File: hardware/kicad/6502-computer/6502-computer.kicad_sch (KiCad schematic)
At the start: 1 part, among them U1 W65C02

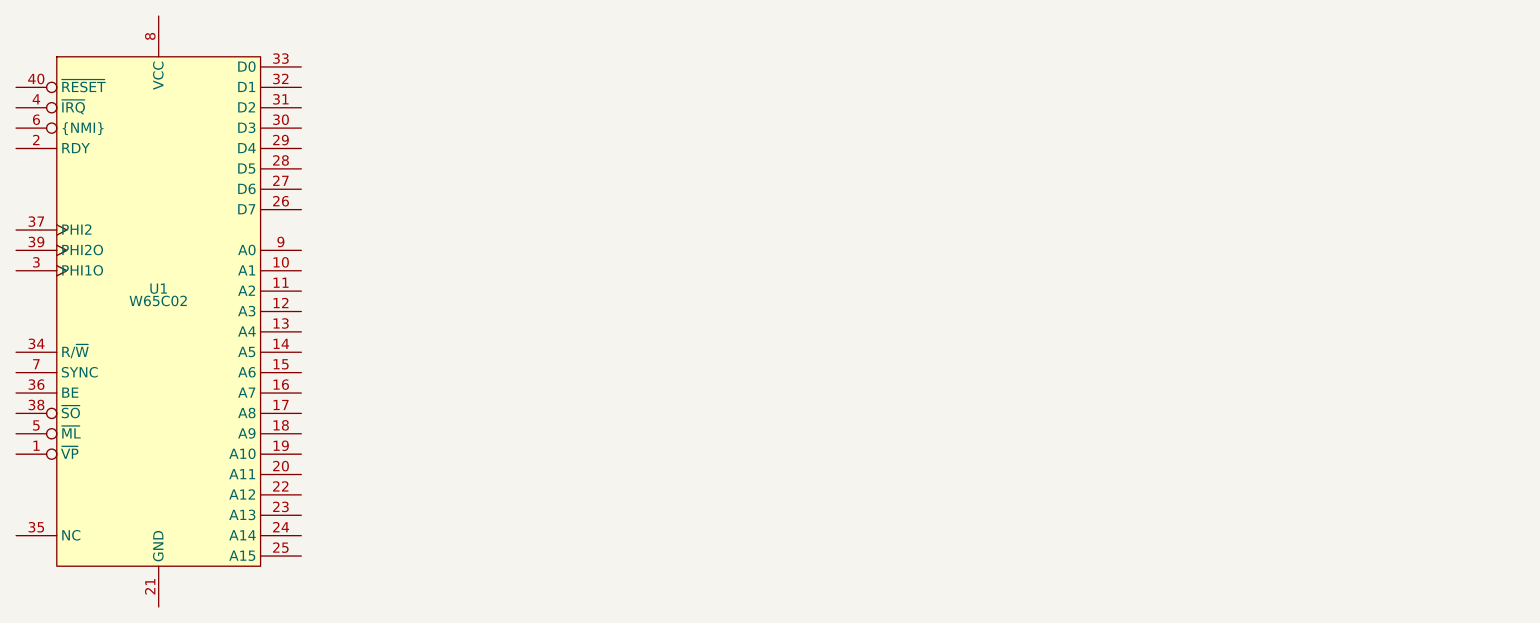
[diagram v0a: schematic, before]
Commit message: added 65c22 symbol and added it to schematics
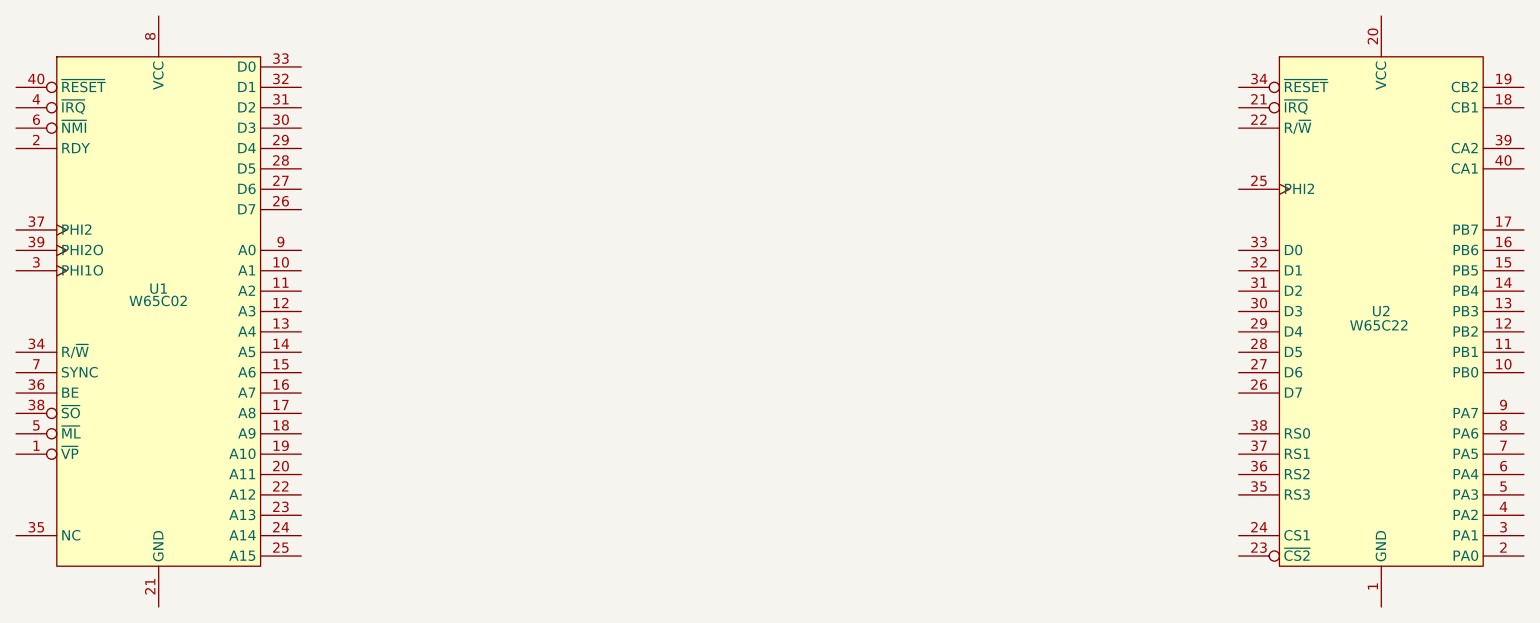
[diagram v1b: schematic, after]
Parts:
- added U2: W65C22, Package_DIP:DIP-40_W15.24mm, symbol 6502-computer:W65C22
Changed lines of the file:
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@@
 			)
+		)
+		(pin "26"
+		)
+		(pin "10"
+		)
+		(pin "31"
+		)
+		(pin "39"
+		)
+		(pin "37"
+		)
+		(pin "20"
+		)
+		(pin "35"
+		)
+		(pin "6"
+		)
+		(pin "19"
+		)
+		(pin "4"
+		)
+		(pin "40"
+		)
+		(pin "33"
+		)
+		(pin "8"
+		)
+		(pin "18"
+		)
+		(pin "21"
+		)
+		(pin "32"
+		)
+		(pin "15"
+		)
+		(pin "23"
+		)
+		(pin "27"
+		)
+		(pin "2"
+		)
+		(pin "3"
+		)
+		(pin "25"
+		)
+		(pin "7"
+		)
+		(pin "36"
+		)
+		(pin "16"
+		)
+		(pin "38"
+		)
+		(pin "28"
+		)
+		(pin "5"
 		)
 		(pin "17"
 		)
+		(pin "29"
+		)
+		(pin "1"
+		)
+		(pin "30"
+		)
 		(pin "12"
 		)
-		(pin "20"
-		)
-		(pin "40"
+		(pin "11"
+		)
+		(pin "14"
+		)
+		(pin "13"
 		)
 		(pin "34"
@@
 		(pin "9"
 		)
-		(pin "11"
-		)
-		(pin "30"
-		)
-		(pin "36"
-		)
-		(pin "25"
-		)
-		(pin "27"
-		)
-		(pin "32"
-		)
-		(pin "33"
-		)
-		(pin "38"
-		)
-		(pin "7"
-		)
-		(pin "19"
-		)
-		(pin "14"
-		)
-		(pin "10"
-		)
-		(pin "26"
-		)
-		(pin "3"
-		)
-		(pin "35"
-		)
-		(pin "5"
-		)
-		(pin "6"
-		)
-		(pin "39"
-		)
 		(pin "24"
 		)
-		(pin "28"
-		)
-		(pin "16"
-		)
-		(pin "1"
-		)
-		(pin "31"
-		)
-		(pin "29"
-		)
 		(pin "22"
-		)
-		(pin "8"
-		)
-		(pin "18"
-		)
-		(pin "23"
-		)
-		(pin "15"
-		)
-		(pin "21"
-		)
-		(pin "4"
-		)
-		(pin "13"
-		)
-		(pin "37"
-		)
-		(pin "2"
 		)
 		(instances
@@
 					(unit 1)
 				)
+			)
+		)
+	)
+	(symbol
+		(lib_id "6502-computer:W65C22")
+		(at 190.5 50.8 0)
+		(unit 1)
+		(exclude_from_sim no)
+		(in_bom yes)
+		(on_board yes)
+		(dnp no)
+		(fields_autoplaced yes)
+		(property "Reference" "U2"
+			(at 190.5 69.85 0)
+			(do_not_autoplace yes)
+			(effects
+				(font
+					(size 1.27 1.27)
+				)
+			)
+		)
+		(property "Value" "W65C22"
+			(at 190.246 71.628 0)
+			(do_not_autoplace yes)
+			(effects
+				(font
+					(size 1.27 1.27)
+				)
+			)
+		)
+		(property "Footprint" "Package_DIP:DIP-40_W15.24mm"
+			(at 190.5 50.8 0)
+			(effects
+				(font
+					(size 1.27 1.27)
+				)
+				(hide yes)
+			)
+		)
+		(property "Datasheet" "kicad-embed://w65c22.pdf"
+			(at 190.5 50.8 0)
+			(effects
+				(font
+					(size 1.27 1.27)
+				)
+				(hide yes)
+			)
+		)
+		(property "Description" "WDC W65C22 Versatile Interface Adapter, 8-bit I/O, DIP-40, 14 MHz"
+			(at 190.5 50.8 0)
+			(effects
+				(font
+					(size 1.27 1.27)
+				)
+				(hide yes)
+			)
+		)
+		(pin "13"
+		)
+		(pin "16"
+		)
+		(pin "11"
+		)
+		(pin "27"
+		)
+		(pin "9"
+		)
+		(pin "2"
+		)
+		(pin "37"
+		)
+		(pin "38"
+		)
+		(pin "17"
+		)
+		(pin "6"
+		)
+		(pin "29"
+		)
+		(pin "14"
+		)
+		(pin "12"
+		)
+		(pin "36"
+		)
+		(pin "10"
+		)
+		(pin "15"
+		)
+		(pin "1"
+		)
+		(pin "35"
+		)
+		(pin "26"
+		)
+		(pin "5"
+		)
+		(pin "28"
+		)
+		(pin "20"
+		)
+		(pin "18"
+		)
+		(pin "19"
+		)
+		(pin "23"
+		)
+		(pin "40"
+		)
+		(pin "30"
+		)
+		(pin "3"
+		)
+		(pin "39"
+		)
+		(pin "31"
+		)
+		(pin "4"
+		)
+		(pin "32"
+		)
+		(pin "33"
+		)
+		(pin "25"
+		)
+		(pin "22"
+		)
+		(pin "21"
+		)
+		(pin "34"
+		)
+		(pin "24"
+		)
+		(pin "8"
+		)
+		(pin "7"
+		)
+		(instances
+			(project ""
+				(path "/d2aa039e-ce8c-4c7f-9c5c-f02700def471"
+					(reference "U2")
+					(unit 1)
+				)
